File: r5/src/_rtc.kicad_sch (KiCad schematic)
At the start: 9 parts, among them U13 DS3231MZ, U14 74LVC1G07DCK

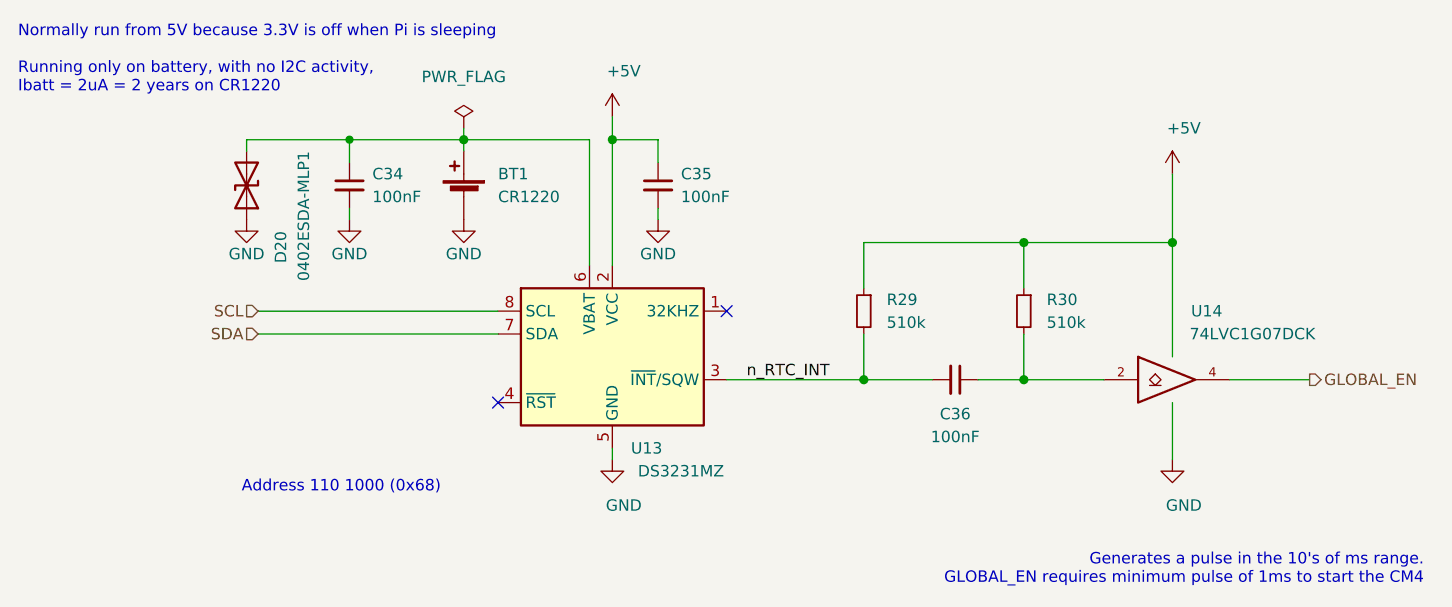
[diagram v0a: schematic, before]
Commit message: Updates to +/-15V supply. Additional output capacitance. Change to smaller inductor packages. Add 0R links to permit isolation of output. Mods to compensation network. Set feedback resistors to datasheet values.
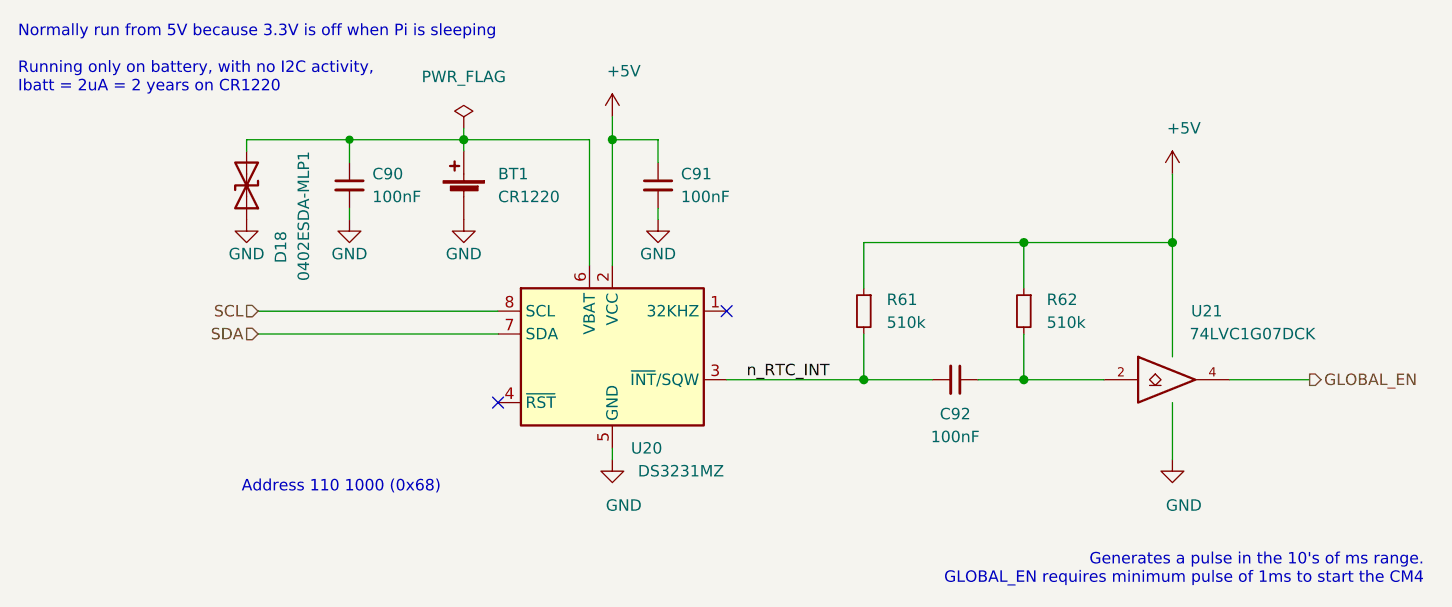
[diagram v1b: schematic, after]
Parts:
- renumbered C34 to C90, C35 to C91, C36 to C92, D20 to D18, R29 to R61, R30 to R62, U13 to U20, U14 to U21
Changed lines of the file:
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@@
   (symbol (lib_id "power:GND") (at 82.55 81.28 0) (unit 1)
     (in_bom yes) (on_board yes) (dnp no)
-    (property "Reference" "#PWR098" (at 82.55 87.63 0)
+    (property "Reference" "#PWR0171" (at 82.55 87.63 0)
       (effects (font (size 1.27 1.27)) hide)
     )
@@
       (project "bugg-main-r5"
         (path "/e3eb514f-6ce4-4abe-ba20-f82f0015628f/41dcda57-f03b-4254-a26d-4b483d171c17"
-          (reference "#PWR098") (unit 1)
+          (reference "#PWR0171") (unit 1)
         )
       )
@@
   (symbol (lib_id "Device:D_TVS") (at 82.55 77.47 270) (mirror x) (unit 1)
     (in_bom yes) (on_board yes) (dnp no)
-    (property "Reference" "D20" (at 86.36 82.55 0)
+    (property "Reference" "D18" (at 86.36 82.55 0)
       (effects (font (size 1.27 1.27)) (justify right))
     )
@@
       (project "bugg-main-r5"
         (path "/e3eb514f-6ce4-4abe-ba20-f82f0015628f/41dcda57-f03b-4254-a26d-4b483d171c17"
-          (reference "D20") (unit 1)
+          (reference "D18") (unit 1)
         )
       )
@@
   (symbol (lib_id "power:GND") (at 123.19 107.95 0) (unit 1)
     (in_bom yes) (on_board yes) (dnp no)
-    (property "Reference" "#PWR0101" (at 123.19 114.3 0)
+    (property "Reference" "#PWR0175" (at 123.19 114.3 0)
       (effects (font (size 1.27 1.27)) hide)
     )
@@
       (project "bugg-main-r5"
         (path "/e3eb514f-6ce4-4abe-ba20-f82f0015628f/41dcda57-f03b-4254-a26d-4b483d171c17"
-          (reference "#PWR0101") (unit 1)
+          (reference "#PWR0175") (unit 1)
         )
       )
@@
   (symbol (lib_id "power:+5V") (at 185.42 76.2 0) (unit 1)
     (in_bom yes) (on_board yes) (dnp no)
-    (property "Reference" "#PWR0103" (at 185.42 80.01 0)
+    (property "Reference" "#PWR0177" (at 185.42 80.01 0)
       (effects (font (size 1.27 1.27)) hide)
     )
@@
       (project "bugg-main-r5"
         (path "/e3eb514f-6ce4-4abe-ba20-f82f0015628f/41dcda57-f03b-4254-a26d-4b483d171c17"
-          (reference "#PWR0103") (unit 1)
+          (reference "#PWR0177") (unit 1)
         )
       )
@@
   (symbol (lib_id "power:GND") (at 93.98 81.28 0) (unit 1)
     (in_bom yes) (on_board yes) (dnp no)
-    (property "Reference" "#PWR0139" (at 93.98 87.63 0)
+    (property "Reference" "#PWR0172" (at 93.98 87.63 0)
       (effects (font (size 1.27 1.27)) hide)
     )
@@
       (project "bugg-main-r5"
         (path "/e3eb514f-6ce4-4abe-ba20-f82f0015628f/41dcda57-f03b-4254-a26d-4b483d171c17"
-          (reference "#PWR0139") (unit 1)
+          (reference "#PWR0172") (unit 1)
         )
       )
@@
   (symbol (lib_id "power:GND") (at 185.42 107.95 0) (unit 1)
     (in_bom yes) (on_board yes) (dnp no)
-    (property "Reference" "#PWR0104" (at 185.42 114.3 0)
+    (property "Reference" "#PWR0178" (at 185.42 114.3 0)
       (effects (font (size 1.27 1.27)) hide)
     )
@@
       (project "bugg-main-r5"
         (path "/e3eb514f-6ce4-4abe-ba20-f82f0015628f/41dcda57-f03b-4254-a26d-4b483d171c17"
-          (reference "#PWR0104") (unit 1)
+          (reference "#PWR0178") (unit 1)
         )
       )
@@
   (symbol (lib_id "Device:C_Small") (at 128.27 77.47 0) (unit 1)
     (in_bom yes) (on_board yes) (dnp no)
-    (property "Reference" "C35" (at 130.81 76.2 0)
+    (property "Reference" "C91" (at 130.81 76.2 0)
       (effects (font (size 1.27 1.27)) (justify left))
     )
@@
       (project "bugg-main-r5"
         (path "/e3eb514f-6ce4-4abe-ba20-f82f0015628f/41dcda57-f03b-4254-a26d-4b483d171c17"
-          (reference "C35") (unit 1)
+          (reference "C91") (unit 1)
         )
       )
@@
   (symbol (lib_id "74xGxx:74LVC1G07") (at 185.42 99.06 0) (unit 1)
     (in_bom yes) (on_board yes) (dnp no)
-    (property "Reference" "U14" (at 189.23 91.44 0)
+    (property "Reference" "U21" (at 189.23 91.44 0)
       (effects (font (size 1.27 1.27)))
     )
@@
       (project "bugg-main-r5"
         (path "/e3eb514f-6ce4-4abe-ba20-f82f0015628f/41dcda57-f03b-4254-a26d-4b483d171c17"
-          (reference "U14") (unit 1)
+          (reference "U21") (unit 1)
         )
       )
@@
   (symbol (lib_id "power:+5V") (at 123.19 69.85 0) (unit 1)
     (in_bom yes) (on_board yes) (dnp no)
-    (property "Reference" "#PWR0100" (at 123.19 73.66 0)
+    (property "Reference" "#PWR0174" (at 123.19 73.66 0)
       (effects (font (size 1.27 1.27)) hide)
     )
@@
       (project "bugg-main-r5"
         (path "/e3eb514f-6ce4-4abe-ba20-f82f0015628f/41dcda57-f03b-4254-a26d-4b483d171c17"
-          (reference "#PWR0100") (unit 1)
+          (reference "#PWR0174") (unit 1)
         )
       )
@@
   (symbol (lib_id "Device:C_Small") (at 161.29 99.06 270) (unit 1)
     (in_bom yes) (on_board yes) (dnp no)
-    (property "Reference" "C36" (at 161.29 102.87 90)
+    (property "Reference" "C92" (at 161.29 102.87 90)
       (effects (font (size 1.27 1.27)))
     )
@@
       (project "bugg-main-r5"
         (path "/e3eb514f-6ce4-4abe-ba20-f82f0015628f/41dcda57-f03b-4254-a26d-4b483d171c17"
-          (reference "C36") (unit 1)
+          (reference "C92") (unit 1)
         )
       )
@@
   (symbol (lib_id "power:GND") (at 106.68 81.28 0) (unit 1)
     (in_bom yes) (on_board yes) (dnp no)
-    (property "Reference" "#PWR099" (at 106.68 87.63 0)
+    (property "Reference" "#PWR0173" (at 106.68 87.63 0)
       (effects (font (size 1.27 1.27)) hide)
     )
@@
       (project "bugg-main-r5"
         (path "/e3eb514f-6ce4-4abe-ba20-f82f0015628f/41dcda57-f03b-4254-a26d-4b483d171c17"
-          (reference "#PWR099") (unit 1)
+          (reference "#PWR0173") (unit 1)
         )
       )
@@
   (symbol (lib_id "Device:R_Small") (at 168.91 91.44 0) (mirror y) (unit 1)
     (in_bom yes) (on_board yes) (dnp no)
-    (property "Reference" "R30" (at 171.45 90.17 0)
+    (property "Reference" "R62" (at 171.45 90.17 0)
       (effects (font (size 1.27 1.27)) (justify right))
     )
@@
       (project "bugg-main-r5"
         (path "/e3eb514f-6ce4-4abe-ba20-f82f0015628f/41dcda57-f03b-4254-a26d-4b483d171c17"
-          (reference "R30") (unit 1)
+          (reference "R62") (unit 1)
         )
       )
@@
   (symbol (lib_id "Device:R_Small") (at 151.13 91.44 0) (mirror y) (unit 1)
     (in_bom yes) (on_board yes) (dnp no)
-    (property "Reference" "R29" (at 153.67 90.17 0)
+    (property "Reference" "R61" (at 153.67 90.17 0)
       (effects (font (size 1.27 1.27)) (justify right))
     )
@@
       (project "bugg-main-r5"
         (path "/e3eb514f-6ce4-4abe-ba20-f82f0015628f/41dcda57-f03b-4254-a26d-4b483d171c17"
-          (reference "R29") (unit 1)
+          (reference "R61") (unit 1)
         )
       )
@@
   (symbol (lib_id "power:PWR_FLAG") (at 106.68 71.12 0) (unit 1)
     (in_bom yes) (on_board yes) (dnp no)
-    (property "Reference" "#FLG0105" (at 106.68 69.215 0)
+    (property "Reference" "#FLG015" (at 106.68 69.215 0)
       (effects (font (size 1.27 1.27)) hide)
     )
@@
       (project "bugg-main-r5"
         (path "/e3eb514f-6ce4-4abe-ba20-f82f0015628f/41dcda57-f03b-4254-a26d-4b483d171c17"
-          (reference "#FLG0105") (unit 1)
+          (reference "#FLG015") (unit 1)
         )
       )
@@
   (symbol (lib_id "Timer_RTC:DS3231MZ") (at 123.19 96.52 0) (unit 1)
     (in_bom yes) (on_board yes) (dnp no)
-    (property "Reference" "U13" (at 127 106.68 0)
+    (property "Reference" "U20" (at 127 106.68 0)
       (effects (font (size 1.27 1.27)))
     )
@@
       (project "bugg-main-r5"
         (path "/e3eb514f-6ce4-4abe-ba20-f82f0015628f/41dcda57-f03b-4254-a26d-4b483d171c17"
-          (reference "U13") (unit 1)
+          (reference "U20") (unit 1)
         )
       )
@@
   (symbol (lib_id "power:GND") (at 128.27 81.28 0) (unit 1)
     (in_bom yes) (on_board yes) (dnp no)
-    (property "Reference" "#PWR0102" (at 128.27 87.63 0)
+    (property "Reference" "#PWR0176" (at 128.27 87.63 0)
       (effects (font (size 1.27 1.27)) hide)
     )
@@
       (project "bugg-main-r5"
         (path "/e3eb514f-6ce4-4abe-ba20-f82f0015628f/41dcda57-f03b-4254-a26d-4b483d171c17"
-          (reference "#PWR0102") (unit 1)
+          (reference "#PWR0176") (unit 1)
         )
       )
@@
   (symbol (lib_id "Device:C_Small") (at 93.98 77.47 0) (unit 1)
     (in_bom yes) (on_board yes) (dnp no)
-    (property "Reference" "C34" (at 96.52 76.2 0)
+    (property "Reference" "C90" (at 96.52 76.2 0)
       (effects (font (size 1.27 1.27)) (justify left))
     )
@@
       (project "bugg-main-r5"
         (path "/e3eb514f-6ce4-4abe-ba20-f82f0015628f/41dcda57-f03b-4254-a26d-4b483d171c17"
-          (reference "C34") (unit 1)
-        )
-      )
+          (reference "C90") (unit 1)
+        )
+      )

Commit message: Fix broken component annotation by importing back from PCB and fixing duplicates.
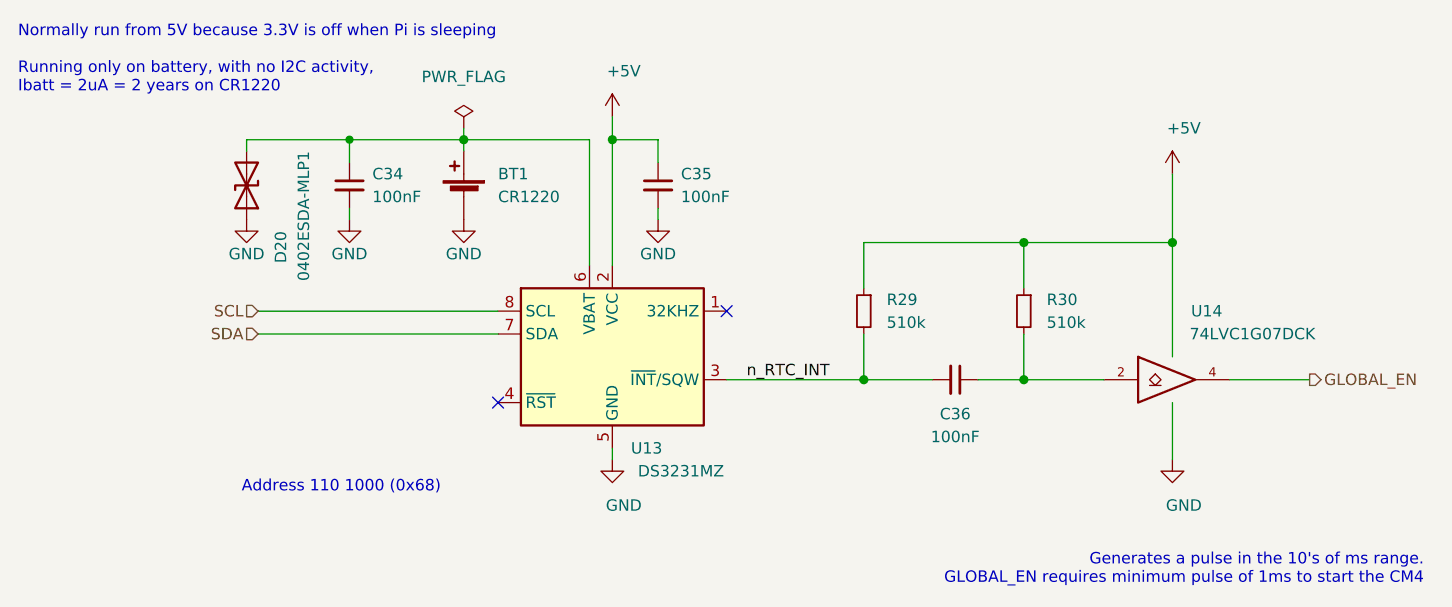
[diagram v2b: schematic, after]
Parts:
- renumbered C90 to C34, C91 to C35, C92 to C36, D18 to D20, R61 to R29, R62 to R30, U20 to U13, U21 to U14
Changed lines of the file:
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@@
   (symbol (lib_id "Device:D_TVS") (at 82.55 77.47 270) (mirror x) (unit 1)
     (in_bom yes) (on_board yes) (dnp no)
-    (property "Reference" "D18" (at 86.36 82.55 0)
+    (property "Reference" "D20" (at 86.36 82.55 0)
       (effects (font (size 1.27 1.27)) (justify right))
     )
@@
       (project "bugg-main-r5"
         (path "/e3eb514f-6ce4-4abe-ba20-f82f0015628f/41dcda57-f03b-4254-a26d-4b483d171c17"
-          (reference "D18") (unit 1)
+          (reference "D20") (unit 1)
         )
       )
@@
   (symbol (lib_id "Device:C_Small") (at 128.27 77.47 0) (unit 1)
     (in_bom yes) (on_board yes) (dnp no)
-    (property "Reference" "C91" (at 130.81 76.2 0)
+    (property "Reference" "C35" (at 130.81 76.2 0)
       (effects (font (size 1.27 1.27)) (justify left))
     )
@@
       (project "bugg-main-r5"
         (path "/e3eb514f-6ce4-4abe-ba20-f82f0015628f/41dcda57-f03b-4254-a26d-4b483d171c17"
-          (reference "C91") (unit 1)
+          (reference "C35") (unit 1)
         )
       )
@@
   (symbol (lib_id "74xGxx:74LVC1G07") (at 185.42 99.06 0) (unit 1)
     (in_bom yes) (on_board yes) (dnp no)
-    (property "Reference" "U21" (at 189.23 91.44 0)
+    (property "Reference" "U14" (at 189.23 91.44 0)
       (effects (font (size 1.27 1.27)))
     )
@@
       (project "bugg-main-r5"
         (path "/e3eb514f-6ce4-4abe-ba20-f82f0015628f/41dcda57-f03b-4254-a26d-4b483d171c17"
-          (reference "U21") (unit 1)
+          (reference "U14") (unit 1)
         )
       )
@@
   (symbol (lib_id "Device:C_Small") (at 161.29 99.06 270) (unit 1)
     (in_bom yes) (on_board yes) (dnp no)
-    (property "Reference" "C92" (at 161.29 102.87 90)
+    (property "Reference" "C36" (at 161.29 102.87 90)
       (effects (font (size 1.27 1.27)))
     )
@@
       (project "bugg-main-r5"
         (path "/e3eb514f-6ce4-4abe-ba20-f82f0015628f/41dcda57-f03b-4254-a26d-4b483d171c17"
-          (reference "C92") (unit 1)
+          (reference "C36") (unit 1)
         )
       )
@@
   (symbol (lib_id "Device:R_Small") (at 168.91 91.44 0) (mirror y) (unit 1)
     (in_bom yes) (on_board yes) (dnp no)
-    (property "Reference" "R62" (at 171.45 90.17 0)
+    (property "Reference" "R30" (at 171.45 90.17 0)
       (effects (font (size 1.27 1.27)) (justify right))
     )
@@
       (project "bugg-main-r5"
         (path "/e3eb514f-6ce4-4abe-ba20-f82f0015628f/41dcda57-f03b-4254-a26d-4b483d171c17"
-          (reference "R62") (unit 1)
+          (reference "R30") (unit 1)
         )
       )
@@
   (symbol (lib_id "Device:R_Small") (at 151.13 91.44 0) (mirror y) (unit 1)
     (in_bom yes) (on_board yes) (dnp no)
-    (property "Reference" "R61" (at 153.67 90.17 0)
+    (property "Reference" "R29" (at 153.67 90.17 0)
       (effects (font (size 1.27 1.27)) (justify right))
     )
@@
       (project "bugg-main-r5"
         (path "/e3eb514f-6ce4-4abe-ba20-f82f0015628f/41dcda57-f03b-4254-a26d-4b483d171c17"
-          (reference "R61") (unit 1)
+          (reference "R29") (unit 1)
         )
       )
@@
   (symbol (lib_id "Timer_RTC:DS3231MZ") (at 123.19 96.52 0) (unit 1)
     (in_bom yes) (on_board yes) (dnp no)
-    (property "Reference" "U20" (at 127 106.68 0)
+    (property "Reference" "U13" (at 127 106.68 0)
       (effects (font (size 1.27 1.27)))
     )
@@
       (project "bugg-main-r5"
         (path "/e3eb514f-6ce4-4abe-ba20-f82f0015628f/41dcda57-f03b-4254-a26d-4b483d171c17"
-          (reference "U20") (unit 1)
+          (reference "U13") (unit 1)
         )
       )
@@
   (symbol (lib_id "Device:C_Small") (at 93.98 77.47 0) (unit 1)
     (in_bom yes) (on_board yes) (dnp no)
-    (property "Reference" "C90" (at 96.52 76.2 0)
+    (property "Reference" "C34" (at 96.52 76.2 0)
       (effects (font (size 1.27 1.27)) (justify left))
     )
@@
       (project "bugg-main-r5"
         (path "/e3eb514f-6ce4-4abe-ba20-f82f0015628f/41dcda57-f03b-4254-a26d-4b483d171c17"
-          (reference "C90") (unit 1)
-        )
-      )
+          (reference "C34") (unit 1)
+        )
+      )
